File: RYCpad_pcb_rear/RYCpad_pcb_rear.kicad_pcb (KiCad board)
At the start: 2 copper layers, 77.2 x 117.6 mm, 6 parts

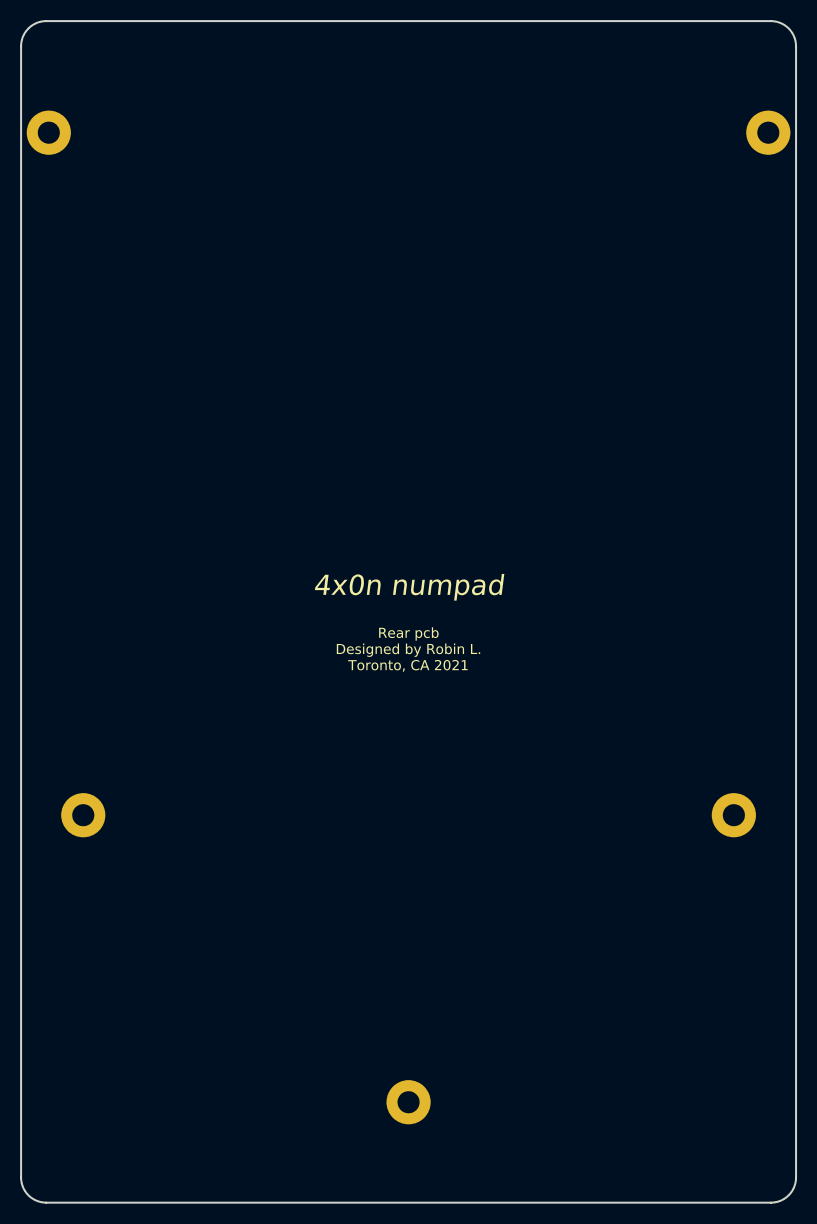
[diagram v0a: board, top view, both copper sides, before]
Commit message: update rear pcb
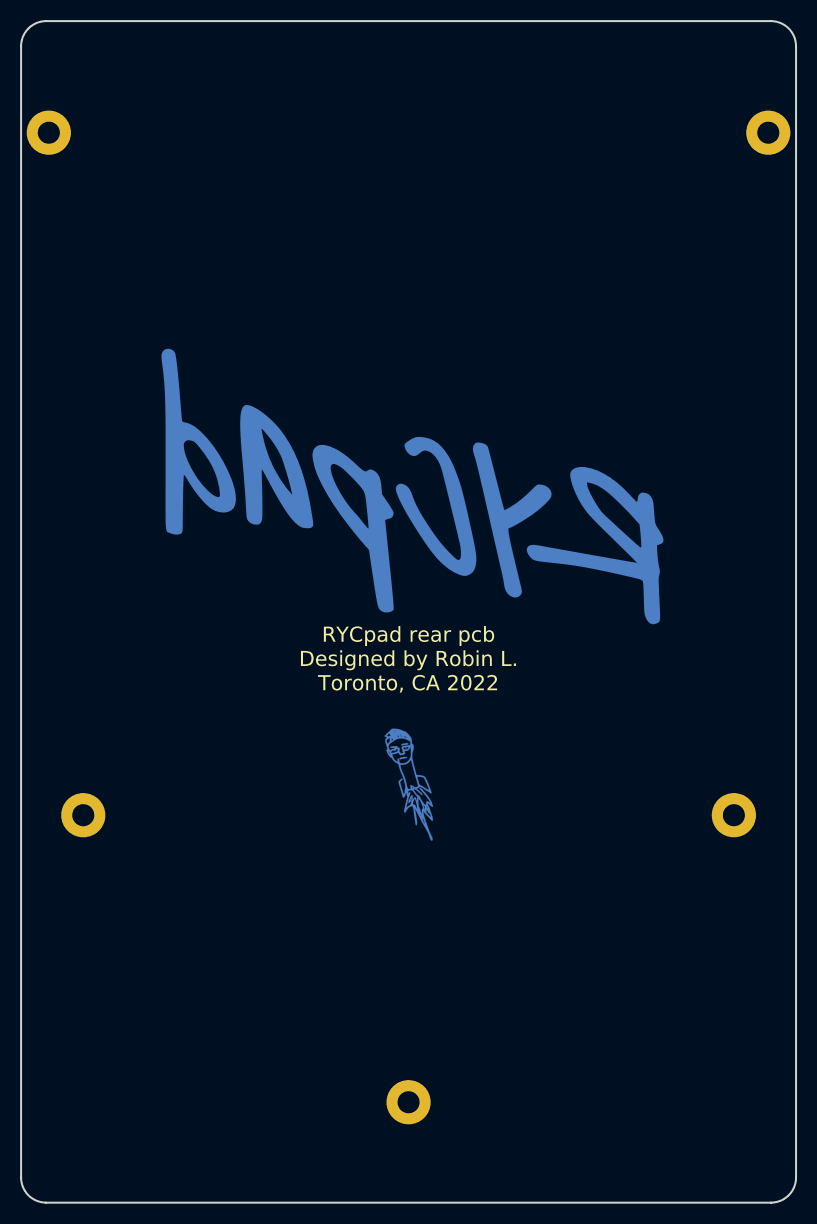
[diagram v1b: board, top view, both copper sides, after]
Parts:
- added G***: LOGO, personal:RYCpad_logo_v0_huge, B.Cu at (0.37, -13.7)
- moved G*** 15.7 mm to (-0.33, 15.7)
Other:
- board text added: "RYCpad rear pcb Designed by Robin L. Toronto, CA 2022"
- board text removed: "4x0n numpad"
- board text removed: "Rear pcb Designed by Robin L. Toronto, CA 2021"

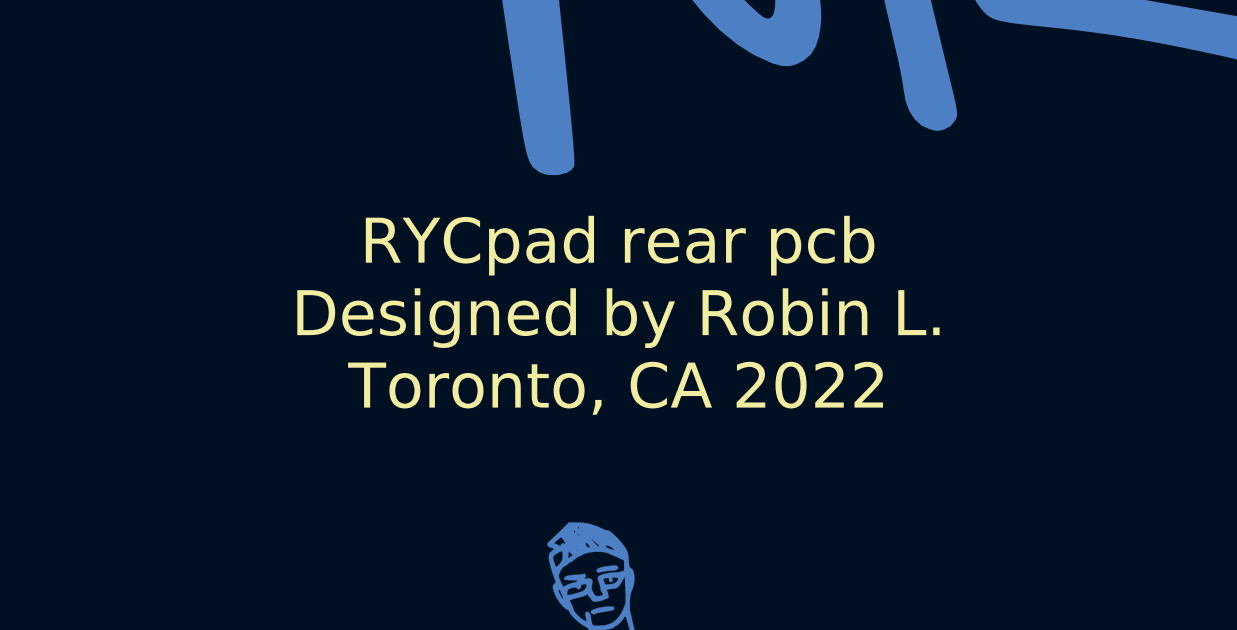
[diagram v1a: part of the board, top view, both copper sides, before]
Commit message: minor changes
- update rear pcb
- thinner silkscreen lines on diode footprint
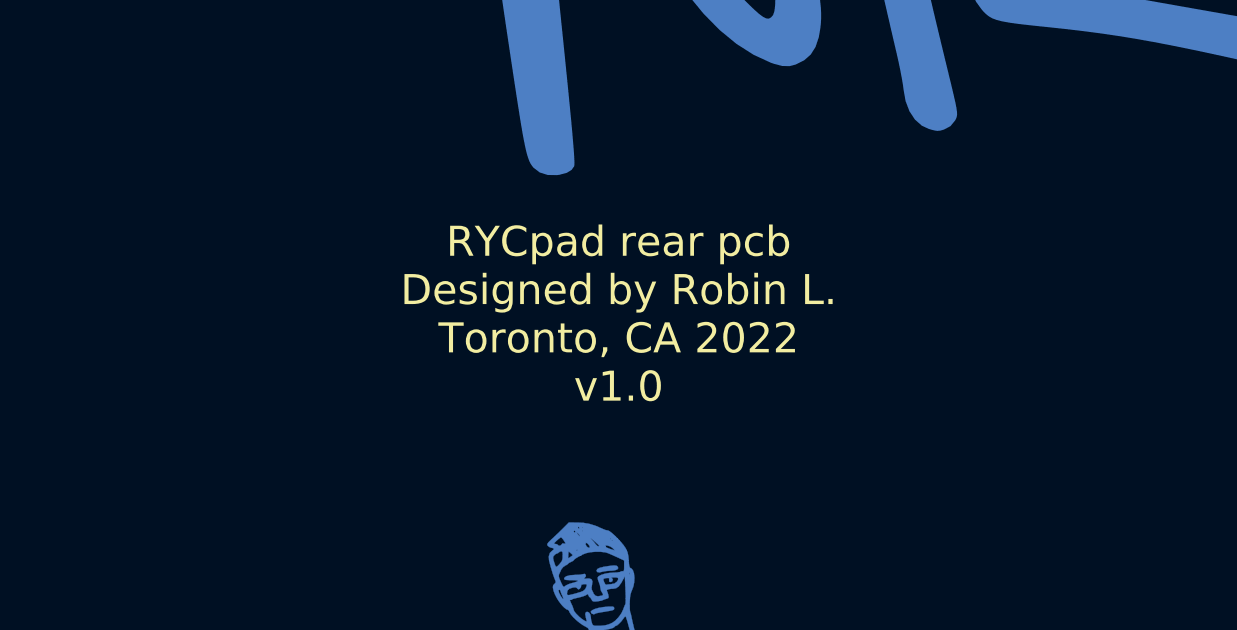
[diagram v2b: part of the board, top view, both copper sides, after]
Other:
- board text added: "RYCpad rear pcb Designed by Robin L. Toronto, CA 2022 v1.0"
- board text removed: "RYCpad rear pcb Designed by Robin L. Toronto, CA 2022"
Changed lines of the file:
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@@
   (gr_arc (start -36.075 57.62485) (mid -37.842767 56.892617) (end -38.575 55.12485) (layer "Edge.Cuts") (width 0.2))
   (gr_line (start 38.575 -57.50595) (end 38.575 55.12485) (layer "Edge.Cuts") (width 0.2))
-  (gr_text "RYCpad rear pcb\nDesigned by Robin L.\nToronto, CA 2022" (at 0 3.5) (layer "F.SilkS")
-    (effects (font (size 1.5 1.5) (thickness 0.3)))
+  (gr_text "RYCpad rear pcb\nDesigned by Robin L.\nToronto, CA 2022\nv1.0" (at 0 3.5) (layer "F.SilkS")
+    (effects (font (size 1 1) (thickness 0.2)))
   )
   (group "" (id 5487601b-81d3-4c70-8f3d-cf9df9c63302)

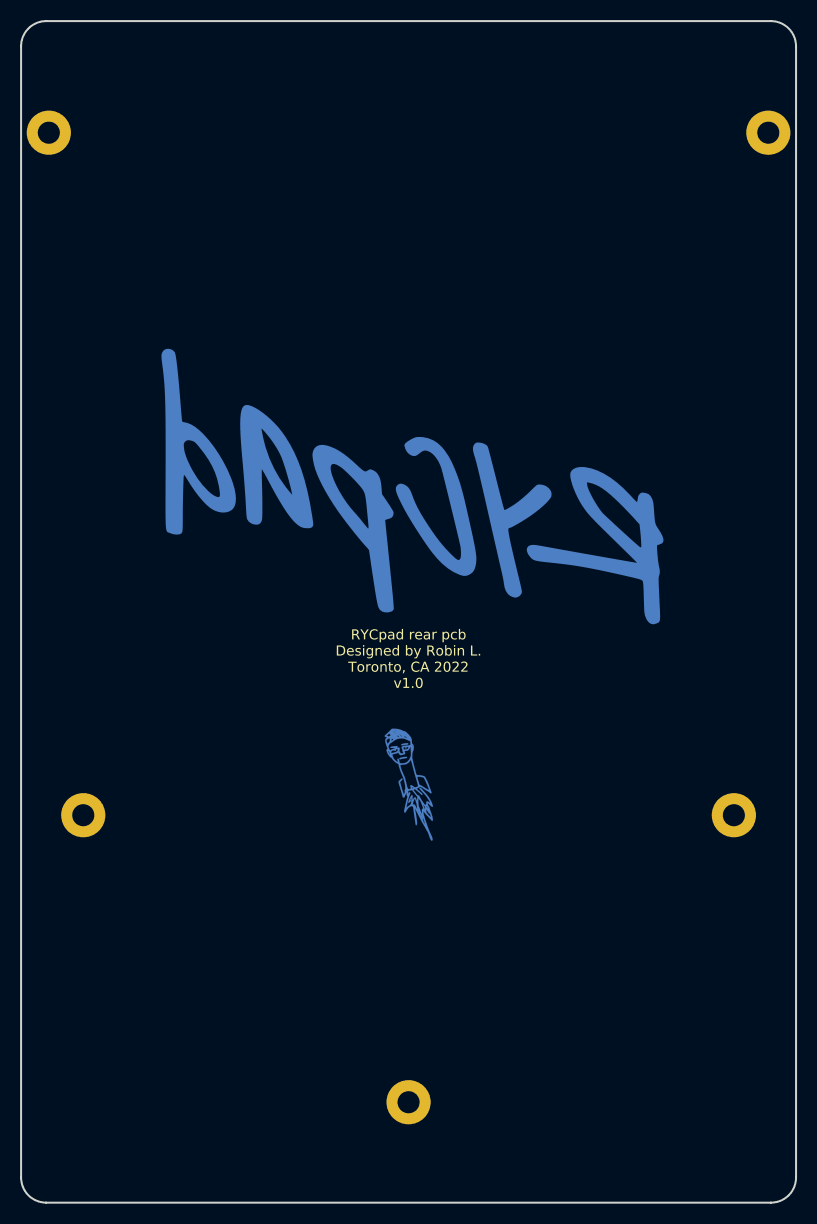
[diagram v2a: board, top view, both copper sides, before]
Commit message: update rear pcb
- Add solder mask windows to allow copper to show even at cheaper board
  shops
- Add copper trim around the edge of the rear pcb
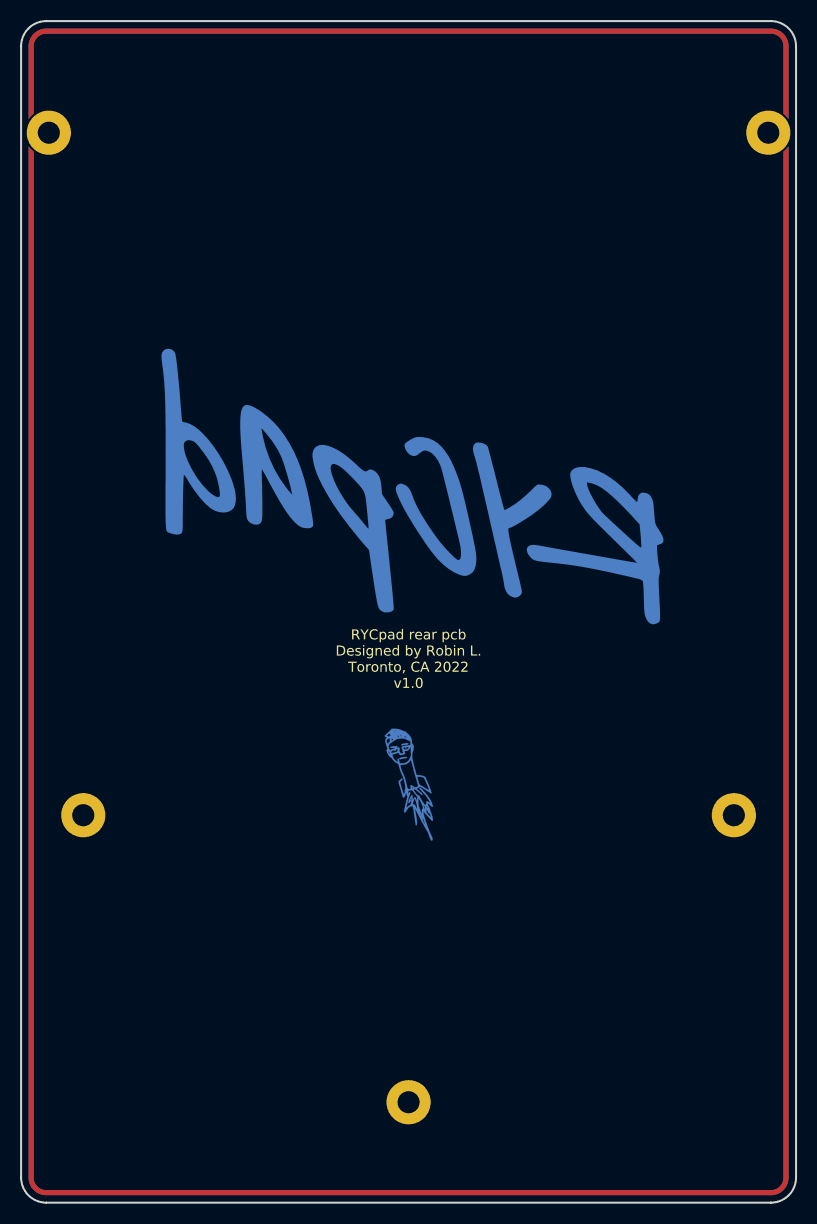
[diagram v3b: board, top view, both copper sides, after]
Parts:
- added G***: LOGO, personal:RYCpad_logo_v0_huge, B.Cu at (0.37, -13.7)
- added G***: LOGO, personal:meme_logo, B.Cu at (-0.33, 15.7)
- added svg2mod (x2): G***, personal:RYCpad_coppertrim_full, F.Cu at (0.00, -1.19)
- added svg2mod (x2): G***, personal:RYCpad_coppertrim_full, B.Cu at (0.00, -1.19)

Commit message: update copper trim
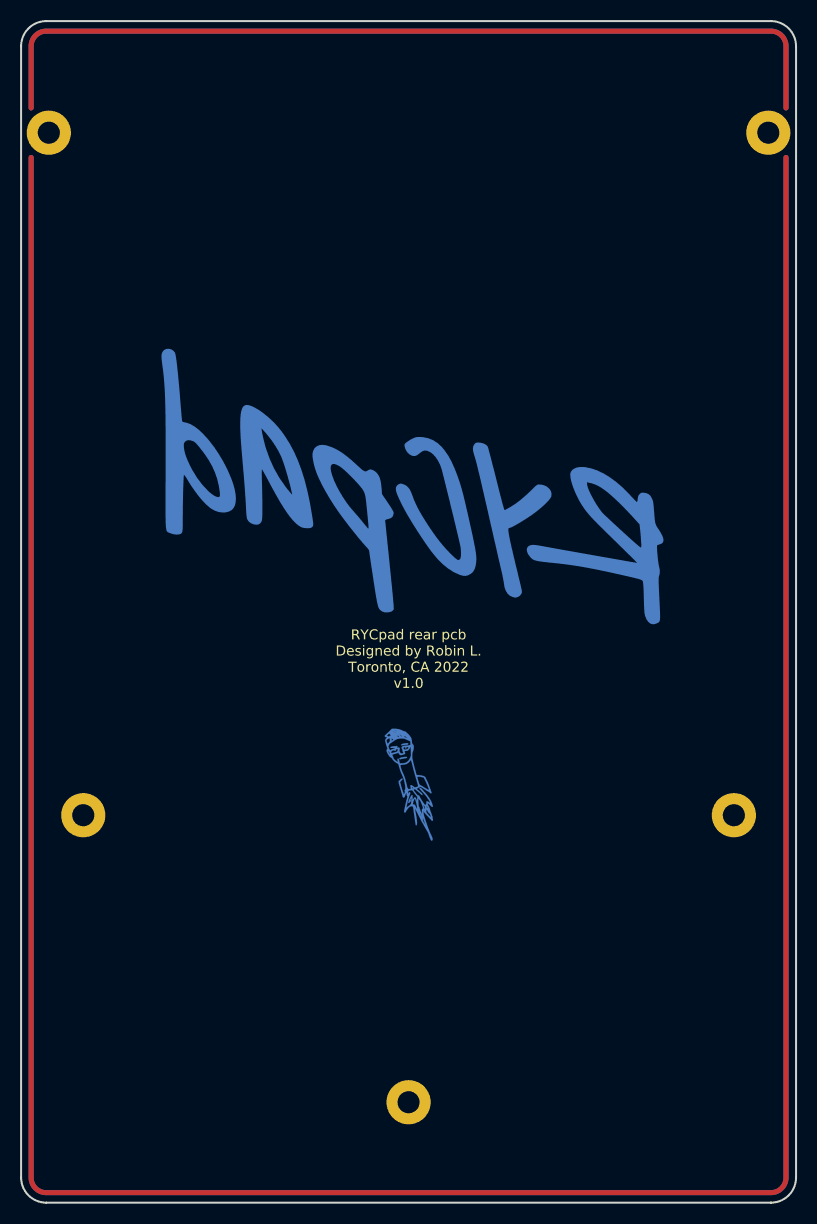
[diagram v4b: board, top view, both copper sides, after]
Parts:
- removed the svg2mod at (0.00, -1.19) (x4)
- added svg2mod (x2): G***, personal:RYCpad_coppertrim_full, F.Cu at (0.00, -1.19)
- added svg2mod (x2): G***, personal:RYCpad_coppertrim_full, B.Cu at (0.00, -1.19)
